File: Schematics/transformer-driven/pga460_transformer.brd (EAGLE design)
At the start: 112.5 x 66.7 mm, 59 parts, among them IC1 PGA460TPWQ1, IC2 PGA460TPWQ1, IC3 PGA460TPWQ1, T1 B78416A2232A003, T2 B78416A2232A003, T3 B78416A2232A003

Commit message: update layout
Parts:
- C12, C19, C2: value 0.1 uF -> 0.1uF
- R14, R22, R6: value 2.7k -> 3k
- moved POWER 6.10 mm to (23.9, -61.7)
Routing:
- net VIN: track 331.4 -> 345.4 mm

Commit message: change connector package
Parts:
- removed MCP2515: (no value), con-lsta:FE07
- added J1: (no value), SparkFun-Connectors:1X07
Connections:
- net 5V: now also J1.1; no longer MCP2515.1
- net CS: now also J1.3; no longer MCP2515.3
- net GND: now also J1.2; no longer MCP2515.2
- net INT: now also J1.7; no longer MCP2515.7
- net MISO: now also J1.4; no longer MCP2515.4
- net MOSI: now also J1.5; no longer MCP2515.5
- net SCLK: now also J1.6; no longer MCP2515.6
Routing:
- net MISO: track 27.6 -> 31.0 mm
- net GND: track 615.5 -> 617.3 mm
- net MOSI: track 41.3 -> 40.2 mm
- net SCLK: track 23.3 -> 24.1 mm
- net 5V: track 158.9 -> 159.6 mm
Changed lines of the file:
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@@
 <attribute name="VALUE" x="54.61" y="-59.436" size="0.6096" layer="27" font="vector" ratio="20" align="top-center"/>
-</element>
-<element name="MCP2515" library="con-lsta" library_urn="urn:adsk.eagle:library:161" package="FE07" package3d_urn="urn:adsk.eagle:package:8223/1" value="" x="73.406" y="-49.022" smashed="yes">
-<attribute name="MF" value="" x="73.406" y="-49.022" size="1.778" layer="27" display="off"/>
-<attribute name="MPN" value="" x="73.406" y="-49.022" size="1.778" layer="27" display="off"/>
-<attribute name="NAME" x="69.596" y="-49.403" size="1.27" layer="25" ratio="10"/>
-<attribute name="OC_FARNELL" value="unknown" x="73.406" y="-49.022" size="1.778" layer="27" display="off"/>
-<attribute name="OC_NEWARK" value="unknown" x="73.406" y="-49.022" size="1.778" layer="27" display="off"/>
-<attribute name="VALUE" x="65.786" y="-51.943" size="1.27" layer="27" ratio="10"/>
 </element>
 <element name="VIN" library="SparkFun-Connectors" package="1X02" value="" x="15.24" y="-55.626" smashed="yes" rot="R180">
@@
 <attribute name="NAME" x="30.988" y="-59.055" size="0.6096" layer="25" font="vector" ratio="20"/>
 <attribute name="VALUE" x="22.606" y="-63.754" size="0.6096" layer="27" font="vector" ratio="20"/>
+</element>
+<element name="J1" library="SparkFun-Connectors" package="1X07" value="" x="64.389" y="-51.689" smashed="yes">
+<attribute name="NAME" x="63.119" y="-50.292" size="0.6096" layer="25" font="vector" ratio="20"/>
+<attribute name="VALUE" x="63.119" y="-53.721" size="0.6096" layer="27" font="vector" ratio="20"/>
 </element>
 </elements>
@@
 <contactref element="C15" pad="1"/>
 <contactref element="C17" pad="1"/>
-<contactref element="MCP2515" pad="2"/>
 <contactref element="POWER" pad="2"/>
 <contactref element="5V/GND" pad="10"/>
@@
 <wire x1="40.64" y1="-44.887" x2="40.386" y2="-44.887" width="0.2032" layer="1"/>
 <wire x1="39.837" y1="-46.187" x2="41.067" y2="-46.187" width="0.2032" layer="1"/>
-<wire x1="68.326" y1="-49.022" x2="62.992" y2="-54.356" width="0.3048" layer="1"/>
-<wire x1="62.992" y1="-54.356" x2="54.356" y2="-54.356" width="0.3048" layer="1"/>
+<wire x1="65.532" y1="-54.356" x2="54.356" y2="-54.356" width="0.3048" layer="1"/>
 <wire x1="54.356" y1="-54.356" x2="49.53" y2="-54.356" width="0.3048" layer="1"/>
 <wire x1="47.99" y1="-26.924" x2="48.498" y2="-26.416" width="0.2032" layer="1"/>
@@
 <wire x1="31.75" y1="-7.874" x2="31.75" y2="-7.366" width="0.3048" layer="1"/>
 <wire x1="45.72" y1="-55.626" x2="48.26" y2="-55.626" width="0.3048" layer="1"/>
-<wire x1="68.326" y1="-49.022" x2="72.517" y2="-44.831" width="0.3048" layer="1"/>
-<wire x1="72.517" y1="-44.831" x2="89.154" y2="-44.831" width="0.3048" layer="1"/>
+<wire x1="72.517" y1="-44.831" x2="72.771" y2="-44.831" width="0.3048" layer="1"/>
+<wire x1="72.771" y1="-44.831" x2="89.154" y2="-44.831" width="0.3048" layer="1"/>
 <wire x1="89.154" y1="-44.831" x2="89.281" y2="-44.831" width="0.2032" layer="1"/>
 <wire x1="34.886" y1="-20.066" x2="37.084" y2="-20.066" width="0.2032" layer="1"/>
@@
 <wire x1="89.154" y1="-44.831" x2="92.456" y2="-41.529" width="0.3048" layer="1"/>
 <wire x1="92.456" y1="-24.892" x2="92.456" y2="-41.529" width="0.3048" layer="1"/>
+<contactref element="J1" pad="2"/>
+<wire x1="66.929" y1="-52.959" x2="66.929" y2="-51.689" width="0.3048" layer="1"/>
+<wire x1="65.532" y1="-54.356" x2="66.929" y2="-52.959" width="0.3048" layer="1"/>
+<wire x1="66.929" y1="-51.689" x2="70.866" y2="-47.752" width="0.3048" layer="1"/>
+<wire x1="70.866" y1="-47.752" x2="70.866" y2="-45.974" width="0.3048" layer="1"/>
+<wire x1="70.866" y1="-45.974" x2="72.009" y2="-44.831" width="0.3048" layer="1"/>
+<wire x1="72.009" y1="-44.831" x2="72.517" y2="-44.831" width="0.3048" layer="1"/>
 <wire x1="22.7" y1="-18.194" x2="22.606" y2="-18.542" width="0" layer="19" extent="1-1"/>
 </signal>
@@
 <contactref element="R19" pad="1"/>
 <contactref element="R18" pad="1"/>
-<contactref element="MCP2515" pad="1"/>
 <contactref element="5V/GND" pad="9"/>
 <contactref element="5V/GND" pad="1"/>
@@
 <contactref element="B1" pad="5V@2"/>
 <contactref element="B1" pad="5V"/>
-<wire x1="65.786" y1="-49.022" x2="62.992" y2="-51.816" width="0.3048" layer="1"/>
-<wire x1="62.992" y1="-51.816" x2="54.102" y2="-51.816" width="0.3048" layer="1"/>
 <wire x1="54.626" y1="-51.816" x2="54.102" y2="-51.816" width="0.2032" layer="1"/>
 <wire x1="53.34" y1="-51.816" x2="54.102" y2="-51.816" width="0.3048" layer="1"/>
@@
 <wire x1="89.916" y1="-24.892" x2="90.424" y2="-25.4" width="0.2032" layer="1"/>
 <wire x1="90.424" y1="-25.4" x2="90.424" y2="-41.656" width="0.3048" layer="1"/>
-<wire x1="70.866" y1="-43.942" x2="65.786" y2="-49.022" width="0.3048" layer="1"/>
 <wire x1="90.424" y1="-41.656" x2="88.138" y2="-43.942" width="0.3048" layer="1"/>
 <wire x1="88.138" y1="-43.942" x2="70.866" y2="-43.942" width="0.3048" layer="1"/>
@@
 <wire x1="41.672" y1="-27.432" x2="41.672" y2="-27.686" width="0.2032" layer="1"/>
 <wire x1="40.894" y1="-53.086" x2="45.72" y2="-53.086" width="0.3048" layer="1"/>
+<contactref element="J1" pad="1"/>
+<wire x1="64.262" y1="-51.816" x2="64.389" y2="-51.689" width="0.3048" layer="1"/>
+<wire x1="54.102" y1="-51.816" x2="64.262" y2="-51.816" width="0.3048" layer="1"/>
+<wire x1="70.866" y1="-43.942" x2="64.389" y2="-50.419" width="0.3048" layer="1"/>
+<wire x1="64.389" y1="-50.419" x2="64.389" y2="-51.689" width="0.3048" layer="1"/>
 </signal>
 <signal name="RX2">
@@
 </signal>
 <signal name="SCLK">
-<contactref element="MCP2515" pad="6"/>
 <contactref element="B1" pad="52"/>
-<wire x1="99.06" y1="-48.006" x2="95.25" y2="-51.816" width="0.2032" layer="1"/>
-<wire x1="78.486" y1="-49.022" x2="81.28" y2="-51.816" width="0.2032" layer="1"/>
-<wire x1="95.25" y1="-51.816" x2="81.28" y2="-51.816" width="0.2032" layer="1"/>
+<wire x1="99.06" y1="-48.006" x2="98.171" y2="-48.895" width="0.2032" layer="1"/>
+<wire x1="98.171" y1="-48.895" x2="78.867" y2="-48.895" width="0.2032" layer="1"/>
+<contactref element="J1" pad="6"/>
+<wire x1="78.867" y1="-48.895" x2="77.089" y2="-50.673" width="0.2032" layer="1"/>
+<wire x1="77.089" y1="-50.673" x2="77.089" y2="-51.689" width="0.2032" layer="1"/>
 </signal>
 <signal name="S1+">
@@
 <wire x1="52.562" y1="-31.242" x2="50.562" y2="-31.242" width="0" layer="19" extent="1-1"/>
 </signal>
-<signal name="INT">
-<contactref element="MCP2515" pad="7"/>
-</signal>
 <signal name="MOSI">
-<contactref element="MCP2515" pad="5"/>
 <contactref element="B1" pad="51"/>
 <wire x1="101.6" y1="-45.466" x2="104.648" y2="-48.514" width="0.2032" layer="1"/>
@@
 <wire x1="104.902" y1="-48.514" x2="104.902" y2="-52.07" width="0.2032" layer="16"/>
 <wire x1="104.902" y1="-52.07" x2="104.14" y2="-52.832" width="0.2032" layer="16"/>
-<wire x1="104.14" y1="-52.832" x2="81.026" y2="-52.832" width="0.2032" layer="16"/>
+<wire x1="104.14" y1="-52.832" x2="81.28" y2="-52.832" width="0.2032" layer="16"/>
 <wire x1="81.026" y1="-52.832" x2="81.28" y2="-52.832" width="0.2032" layer="16"/>
 <via x="81.28" y="-52.832" extent="1-16" drill="0.35"/>
-<wire x1="81.28" y1="-52.832" x2="81.026" y2="-53.086" width="0.2032" layer="1"/>
-<wire x1="81.026" y1="-53.086" x2="77.216" y2="-53.086" width="0.2032" layer="1"/>
-<wire x1="75.946" y1="-49.022" x2="75.946" y2="-51.816" width="0.2032" layer="1"/>
-<wire x1="77.216" y1="-53.086" x2="75.946" y2="-51.816" width="0.2032" layer="1"/>
+<wire x1="81.28" y1="-52.832" x2="80.772" y2="-53.34" width="0.2032" layer="1"/>
+<wire x1="80.772" y1="-53.34" x2="75.692" y2="-53.34" width="0.2032" layer="1"/>
+<wire x1="74.676" y1="-52.324" x2="75.692" y2="-53.34" width="0.2032" layer="1"/>
+<contactref element="J1" pad="5"/>
+<wire x1="74.549" y1="-51.689" x2="74.676" y2="-51.816" width="0.2032" layer="1"/>
+<wire x1="74.676" y1="-51.816" x2="74.676" y2="-52.324" width="0.2032" layer="1"/>
 </signal>
 <signal name="MISO">
-<contactref element="MCP2515" pad="4"/>
 <contactref element="B1" pad="50"/>
 <wire x1="99.06" y1="-45.466" x2="98.171" y2="-46.355" width="0.2032" layer="1"/>
 <wire x1="98.171" y1="-46.355" x2="98.044" y2="-46.482" width="0.2032" layer="1"/>
-<wire x1="98.171" y1="-46.355" x2="75.565" y2="-46.355" width="0.2032" layer="1"/>
-<wire x1="75.565" y1="-46.355" x2="73.406" y2="-48.514" width="0.3048" layer="1"/>
-<wire x1="73.406" y1="-48.514" x2="73.406" y2="-49.022" width="0.3048" layer="1"/>
+<contactref element="J1" pad="4"/>
+<wire x1="72.009" y1="-49.657" x2="72.009" y2="-51.689" width="0.2032" layer="1"/>
+<wire x1="98.171" y1="-46.355" x2="75.311" y2="-46.355" width="0.2032" layer="1"/>
+<wire x1="75.311" y1="-46.355" x2="72.009" y2="-49.657" width="0.2032" layer="1"/>
 </signal>
 <signal name="CS">
-<contactref element="MCP2515" pad="3"/>
 <contactref element="B1" pad="53"/>
 <wire x1="101.6" y1="-48.006" x2="102.108" y2="-48.006" width="0.2032" layer="1"/>
@@
 <wire x1="103.632" y1="-49.53" x2="103.632" y2="-52.324" width="0.2032" layer="1"/>
 <wire x1="103.632" y1="-52.324" x2="101.854" y2="-54.102" width="0.2032" layer="1"/>
-<wire x1="101.854" y1="-54.102" x2="74.168" y2="-54.102" width="0.2032" layer="1"/>
-<wire x1="70.866" y1="-49.022" x2="70.866" y2="-50.8" width="0.2032" layer="1"/>
-<wire x1="74.168" y1="-54.102" x2="70.866" y2="-50.8" width="0.2032" layer="1"/>
+<wire x1="101.854" y1="-54.102" x2="70.358" y2="-54.102" width="0.2032" layer="1"/>
+<contactref element="J1" pad="3"/>
+<wire x1="69.469" y1="-53.213" x2="69.469" y2="-51.689" width="0.2032" layer="1"/>
+<wire x1="70.358" y1="-54.102" x2="69.469" y2="-53.213" width="0.2032" layer="1"/>
 </signal>
 <signal name="SCLK1">
@@
 <wire x1="45.709" y1="-34.533" x2="46.563" y2="-34.533" width="0.2032" layer="1"/>
 </signal>
+<signal name="INT">
+<contactref element="J1" pad="7"/>
+</signal>
 </signals>

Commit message: change connector package
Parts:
- renumbered J1 to MCP2515
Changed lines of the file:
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@@
 <layer number="23" name="tOrigins" color="15" fill="1" visible="yes" active="yes"/>
 <layer number="24" name="bOrigins" color="15" fill="1" visible="no" active="yes"/>
-<layer number="25" name="tNames" color="7" fill="1" visible="yes" active="yes"/>
+<layer number="25" name="tNames" color="7" fill="1" visible="no" active="yes"/>
 <layer number="26" name="bNames" color="7" fill="1" visible="no" active="yes"/>
 <layer number="27" name="tValues" color="7" fill="1" visible="no" active="yes"/>
@@
 <layer number="49" name="Reference" color="7" fill="1" visible="yes" active="yes"/>
 <layer number="50" name="dxf" color="7" fill="1" visible="no" active="no"/>
-<layer number="51" name="tDocu" color="7" fill="1" visible="yes" active="yes"/>
+<layer number="51" name="tDocu" color="7" fill="1" visible="no" active="yes"/>
 <layer number="52" name="bDocu" color="7" fill="1" visible="yes" active="yes"/>
 <layer number="53" name="tGND_GNDA" color="7" fill="9" visible="no" active="no"/>
@@
 <attribute name="VALUE" x="22.606" y="-63.754" size="0.6096" layer="27" font="vector" ratio="20"/>
 </element>
-<element name="J1" library="SparkFun-Connectors" package="1X07" value="" x="64.389" y="-51.689" smashed="yes">
+<element name="MCP2515" library="SparkFun-Connectors" package="1X07" value="" x="64.389" y="-51.689" smashed="yes">
 <attribute name="NAME" x="63.119" y="-50.292" size="0.6096" layer="25" font="vector" ratio="20"/>
 <attribute name="VALUE" x="63.119" y="-53.721" size="0.6096" layer="27" font="vector" ratio="20"/>
@@
 <wire x1="89.154" y1="-44.831" x2="92.456" y2="-41.529" width="0.3048" layer="1"/>
 <wire x1="92.456" y1="-24.892" x2="92.456" y2="-41.529" width="0.3048" layer="1"/>
-<contactref element="J1" pad="2"/>
+<contactref element="MCP2515" pad="2"/>
 <wire x1="66.929" y1="-52.959" x2="66.929" y2="-51.689" width="0.3048" layer="1"/>
 <wire x1="65.532" y1="-54.356" x2="66.929" y2="-52.959" width="0.3048" layer="1"/>
@@
 <wire x1="41.672" y1="-27.432" x2="41.672" y2="-27.686" width="0.2032" layer="1"/>
 <wire x1="40.894" y1="-53.086" x2="45.72" y2="-53.086" width="0.3048" layer="1"/>
-<contactref element="J1" pad="1"/>
+<contactref element="MCP2515" pad="1"/>
 <wire x1="64.262" y1="-51.816" x2="64.389" y2="-51.689" width="0.3048" layer="1"/>
 <wire x1="54.102" y1="-51.816" x2="64.262" y2="-51.816" width="0.3048" layer="1"/>
@@
 <wire x1="99.06" y1="-48.006" x2="98.171" y2="-48.895" width="0.2032" layer="1"/>
 <wire x1="98.171" y1="-48.895" x2="78.867" y2="-48.895" width="0.2032" layer="1"/>
-<contactref element="J1" pad="6"/>
+<contactref element="MCP2515" pad="6"/>
 <wire x1="78.867" y1="-48.895" x2="77.089" y2="-50.673" width="0.2032" layer="1"/>
 <wire x1="77.089" y1="-50.673" x2="77.089" y2="-51.689" width="0.2032" layer="1"/>
@@
 <wire x1="80.772" y1="-53.34" x2="75.692" y2="-53.34" width="0.2032" layer="1"/>
 <wire x1="74.676" y1="-52.324" x2="75.692" y2="-53.34" width="0.2032" layer="1"/>
-<contactref element="J1" pad="5"/>
+<contactref element="MCP2515" pad="5"/>
 <wire x1="74.549" y1="-51.689" x2="74.676" y2="-51.816" width="0.2032" layer="1"/>
 <wire x1="74.676" y1="-51.816" x2="74.676" y2="-52.324" width="0.2032" layer="1"/>
@@
 <wire x1="99.06" y1="-45.466" x2="98.171" y2="-46.355" width="0.2032" layer="1"/>
 <wire x1="98.171" y1="-46.355" x2="98.044" y2="-46.482" width="0.2032" layer="1"/>
-<contactref element="J1" pad="4"/>
+<contactref element="MCP2515" pad="4"/>
 <wire x1="72.009" y1="-49.657" x2="72.009" y2="-51.689" width="0.2032" layer="1"/>
 <wire x1="98.171" y1="-46.355" x2="75.311" y2="-46.355" width="0.2032" layer="1"/>
@@
 <wire x1="103.632" y1="-52.324" x2="101.854" y2="-54.102" width="0.2032" layer="1"/>
 <wire x1="101.854" y1="-54.102" x2="70.358" y2="-54.102" width="0.2032" layer="1"/>
-<contactref element="J1" pad="3"/>
+<contactref element="MCP2515" pad="3"/>
 <wire x1="69.469" y1="-53.213" x2="69.469" y2="-51.689" width="0.2032" layer="1"/>
 <wire x1="70.358" y1="-54.102" x2="69.469" y2="-53.213" width="0.2032" layer="1"/>
@@
 </signal>
 <signal name="INT">
-<contactref element="J1" pad="7"/>
+<contactref element="MCP2515" pad="7"/>
 </signal>
 </signals>

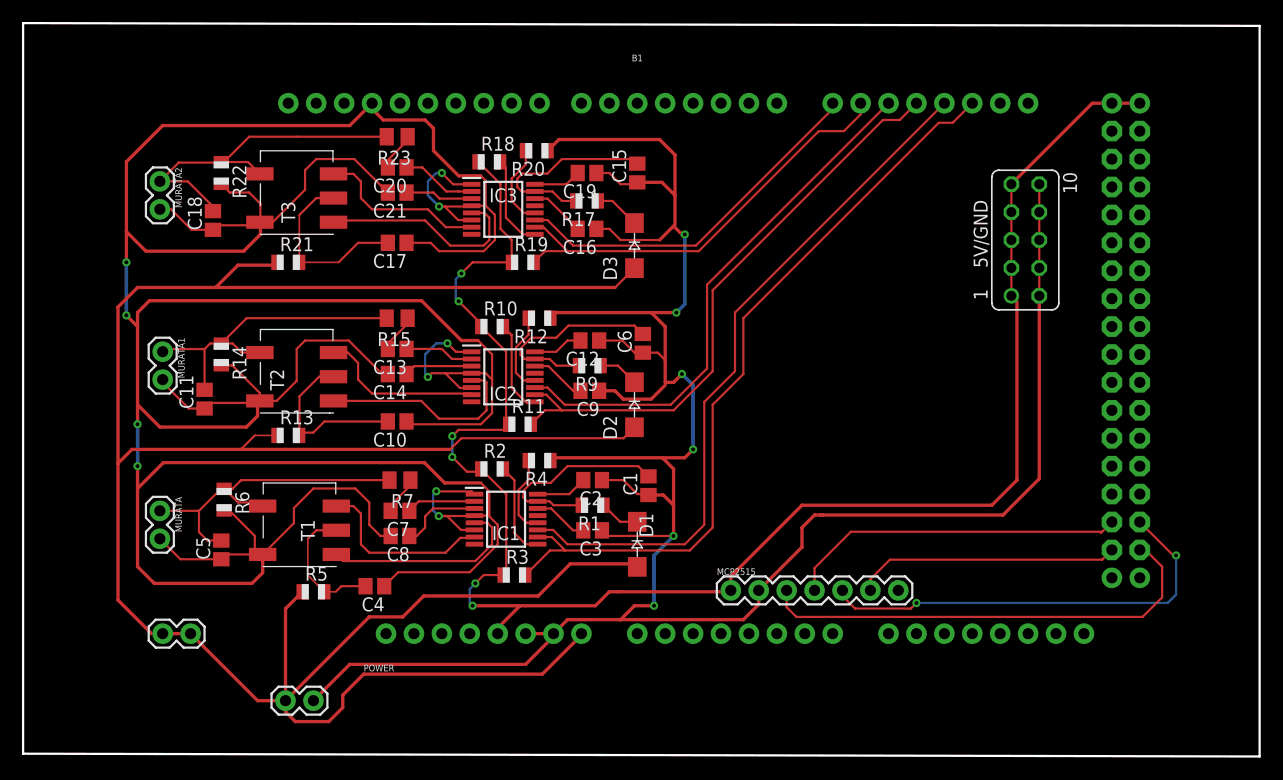
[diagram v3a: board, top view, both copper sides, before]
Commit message: change pga460
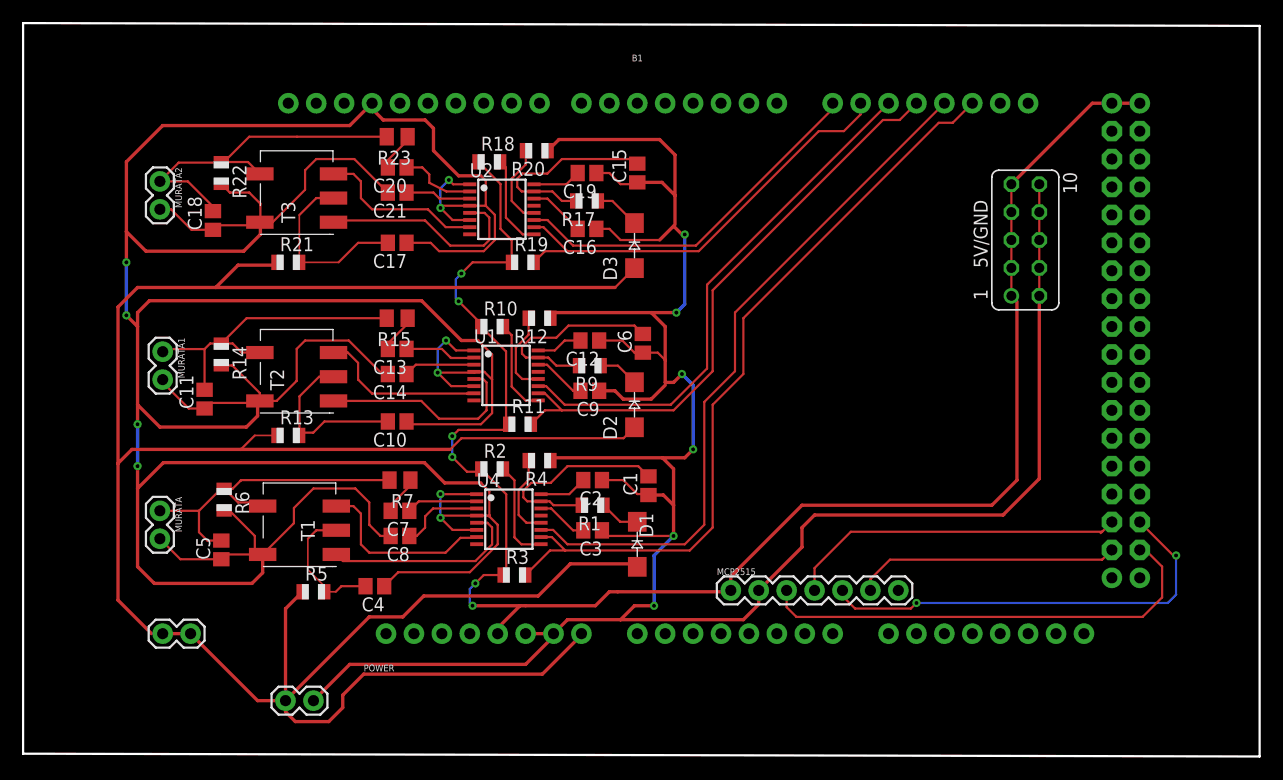
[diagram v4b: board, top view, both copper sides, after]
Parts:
- removed IC1, IC2, IC3: PGA460TPWQ1, PGA460TPWQ1:SOP65P640X120-16N
- added U1, U2, U4: PGA460, texas:TSSOP16
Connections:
- net AVDD1: now also U4.16; no longer IC1.16
- net AVDD2: now also U1.16; no longer IC2.16
- net AVDD3: now also U2.16; no longer IC3.16
- net GND: now also U1.1, U1.4, U1.6, U2.1, U2.4, U2.6, U4.1, U4.4, U4.6; no longer IC1.1, IC1.4, IC1.6, IC2.1, IC2.4, IC2.6, IC3.1, IC3.4, IC3.6
- net INN_1: now also U4.3; no longer IC1.3
- net INN_2: now also U1.3; no longer IC2.3
- net INN_3: now also U2.3; no longer IC3.3
- net INP_1: now also U4.2; no longer IC1.2
- net INP_2: now also U1.2; no longer IC2.2
- net INP_3: now also U2.2; no longer IC3.2
- net IOREG1: now also U4.14; no longer IC1.14
- net IOREG2: now also U1.14; no longer IC2.14
- net IOREG3: now also U2.14; no longer IC3.14
- net OUTA_1: now also U4.5; no longer IC1.5
- net OUTA_2: now also U1.5; no longer IC2.5
- net OUTA_3: now also U2.5; no longer IC3.5
- net OUTB_1: now also U4.7; no longer IC1.7
- net OUTB_2: now also U1.7; no longer IC2.7
- net OUTB_3: now also U2.7; no longer IC3.7
- net RX1: now also U4.10; no longer IC1.10
- net RX2: now also U1.10; no longer IC2.10
- net RX3: now also U2.10; no longer IC3.10
- net SCLK1: now also U4.12; no longer IC1.12
- net SCLK2: now also U1.12; no longer IC2.12
- net SCLK3: now also U2.12; no longer IC3.12
- net TEST1: no longer IC1.9
- net TEST2: no longer IC2.9
- net TEST3: no longer IC3.9
- net TX1: now also U4.11; no longer IC1.11
- net TX2: now also U1.11; no longer IC2.11
- net TX3: now also U2.11; no longer IC3.11
- net VIN: now also U1.15, U2.15, U4.15; no longer IC1.15, IC2.15, IC3.15
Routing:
- net GND: track 617.3 -> 612.9 mm
- net N$2: track 0.00 -> 1.40 mm
- net N$1: track 0.00 -> 1.27 mm
- net TEST3: track 8.54 -> 7.44 mm
- net TEST2: track 8.54 -> 7.56 mm
- net TEST1: track 8.80 -> 9.58 mm
